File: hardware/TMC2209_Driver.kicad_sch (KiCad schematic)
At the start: 31 parts, among them J1 PCIe_Stepper, J2 Conn_01x04_Male, U1 TMC2209-LA, U2 74LVC1G06, U3 24LC02

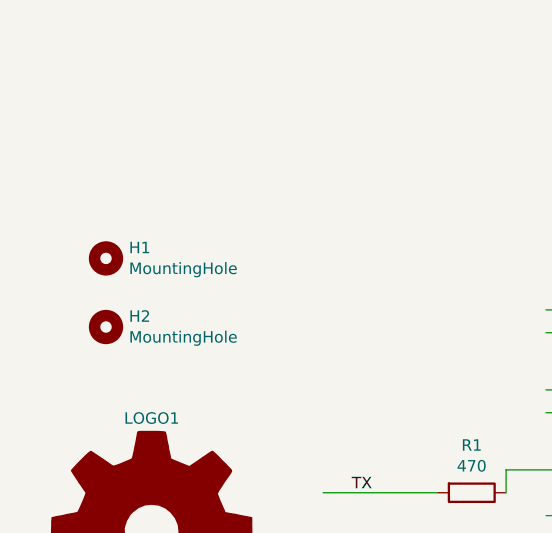
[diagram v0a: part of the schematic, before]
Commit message: Update of PCBs
- added tooling holes
- added order number location under components

Updated projects:
- DRV-Stepstick
- TMC2209
- TMC2130
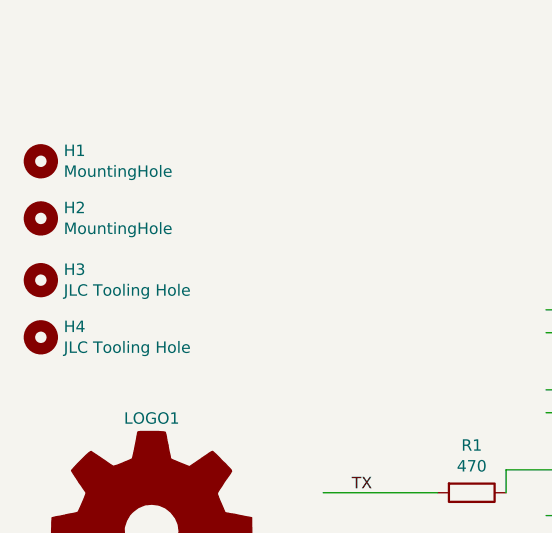
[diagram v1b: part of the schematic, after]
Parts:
- added H3, H4: JLC Tooling Hole, PrntrBoardV2:JLC_Tool_hole, symbol Mechanical:MountingHole
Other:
- moved on the sheet: H1, H2
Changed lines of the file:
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@@
   (junction (at 254 91.44) (diameter 1.016) (color 0 0 0 0))
   (junction (at 254 93.98) (diameter 1.016) (color 0 0 0 0))
+  (no_connect (at 101.6 88.9))
   (no_connect (at 101.6 99.06))
   (no_connect (at 120.65 68.58))
-  (no_connect (at 101.6 88.9))
   (wire (pts (xy 71.755 93.98) (xy 59.055 93.98))
     (stroke (width 0) (type solid) (color 0 0 0 0))
@@
     )
   )
-  (symbol (lib_id "Mechanical:MountingHole") (at 34.925 67.945 0) (unit 1)
+  (symbol (lib_id "Mechanical:MountingHole") (at 27.686 57.15 0) (unit 1)
     (in_bom no) (on_board yes)
-    (property "Reference" "H1" (id 0) (at 37.465 66.7766 0)
-      (effects (font (size 1.27 1.27)) (justify left))
-    )
-    (property "Value" "MountingHole" (id 1) (at 37.465 69.088 0)
-      (effects (font (size 1.27 1.27)) (justify left))
-    )
-    (property "Footprint" "MountingHole:MountingHole_2.7mm_M2.5" (id 2) (at 34.925 67.945 0)
-      (effects (font (size 1.27 1.27)) hide)
-    )
-    (property "Datasheet" "~" (id 3) (at 34.925 67.945 0)
-      (effects (font (size 1.27 1.27)) hide)
-    )
-  )
-  (symbol (lib_id "Mechanical:MountingHole") (at 34.925 75.565 0) (unit 1)
+    (property "Reference" "H1" (id 0) (at 30.226 55.9816 0)
+      (effects (font (size 1.27 1.27)) (justify left))
+    )
+    (property "Value" "MountingHole" (id 1) (at 30.226 58.293 0)
+      (effects (font (size 1.27 1.27)) (justify left))
+    )
+    (property "Footprint" "MountingHole:MountingHole_2.7mm_M2.5" (id 2) (at 27.686 57.15 0)
+      (effects (font (size 1.27 1.27)) hide)
+    )
+    (property "Datasheet" "~" (id 3) (at 27.686 57.15 0)
+      (effects (font (size 1.27 1.27)) hide)
+    )
+  )
+  (symbol (lib_id "Mechanical:MountingHole") (at 27.686 63.5 0) (unit 1)
     (in_bom no) (on_board yes)
-    (property "Reference" "H2" (id 0) (at 37.465 74.3966 0)
-      (effects (font (size 1.27 1.27)) (justify left))
-    )
-    (property "Value" "MountingHole" (id 1) (at 37.465 76.708 0)
-      (effects (font (size 1.27 1.27)) (justify left))
-    )
-    (property "Footprint" "MountingHole:MountingHole_2.7mm_M2.5" (id 2) (at 34.925 75.565 0)
-      (effects (font (size 1.27 1.27)) hide)
-    )
-    (property "Datasheet" "~" (id 3) (at 34.925 75.565 0)
+    (property "Reference" "H2" (id 0) (at 30.226 62.3316 0)
+      (effects (font (size 1.27 1.27)) (justify left))
+    )
+    (property "Value" "MountingHole" (id 1) (at 30.226 64.643 0)
+      (effects (font (size 1.27 1.27)) (justify left))
+    )
+    (property "Footprint" "MountingHole:MountingHole_2.7mm_M2.5" (id 2) (at 27.686 63.5 0)
+      (effects (font (size 1.27 1.27)) hide)
+    )
+    (property "Datasheet" "~" (id 3) (at 27.686 63.5 0)
+      (effects (font (size 1.27 1.27)) hide)
+    )
+  )
+  (symbol (lib_id "Mechanical:MountingHole") (at 27.686 70.358 0) (unit 1)
+    (in_bom no) (on_board yes)
+    (property "Reference" "H3" (id 0) (at 30.226 69.1896 0)
+      (effects (font (size 1.27 1.27)) (justify left))
+    )
+    (property "Value" "JLC Tooling Hole" (id 1) (at 30.226 71.501 0)
+      (effects (font (size 1.27 1.27)) (justify left))
+    )
+    (property "Footprint" "PrntrBoardV2:JLC_Tool_hole" (id 2) (at 27.686 70.358 0)
+      (effects (font (size 1.27 1.27)) hide)
+    )
+    (property "Datasheet" "~" (id 3) (at 27.686 70.358 0)
+      (effects (font (size 1.27 1.27)) hide)
+    )
+  )
+  (symbol (lib_id "Mechanical:MountingHole") (at 27.686 76.708 0) (unit 1)
+    (in_bom no) (on_board yes)
+    (property "Reference" "H4" (id 0) (at 30.226 75.5396 0)
+      (effects (font (size 1.27 1.27)) (justify left))
+    )
+    (property "Value" "JLC Tooling Hole" (id 1) (at 30.226 77.851 0)
+      (effects (font (size 1.27 1.27)) (justify left))
+    )
+    (property "Footprint" "PrntrBoardV2:JLC_Tool_hole" (id 2) (at 27.686 76.708 0)
+      (effects (font (size 1.27 1.27)) hide)
+    )
+    (property "Datasheet" "~" (id 3) (at 27.686 76.708 0)
       (effects (font (size 1.27 1.27)) hide)
     )
@@
       (reference "H2") (unit 1) (value "MountingHole") (footprint "MountingHole:MountingHole_2.7mm_M2.5")
     )
+    (path "/8a4a4cd5-bc6b-44ee-9992-df9c568ed381"
+      (reference "H3") (unit 1) (value "JLC Tooling Hole") (footprint "PrntrBoardV2:JLC_Tool_hole")
+    )
+    (path "/fceddb66-7b25-4e7c-b49c-49d422344a12"
+      (reference "H4") (unit 1) (value "JLC Tooling Hole") (footprint "PrntrBoardV2:JLC_Tool_hole")
+    )
     (path "/00000000-0000-0000-0000-00005d9a9126"
